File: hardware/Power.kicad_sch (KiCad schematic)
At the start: 37 parts, among them U10 LDK320ADU120R, U4 TPS563300DRLR, U5 TPS563219ADDFR, U6 LM2940SX-12_NOPB, U7 LM1117IMP-5.0, U8 TLV743P, U9 AP2127N3-1.5

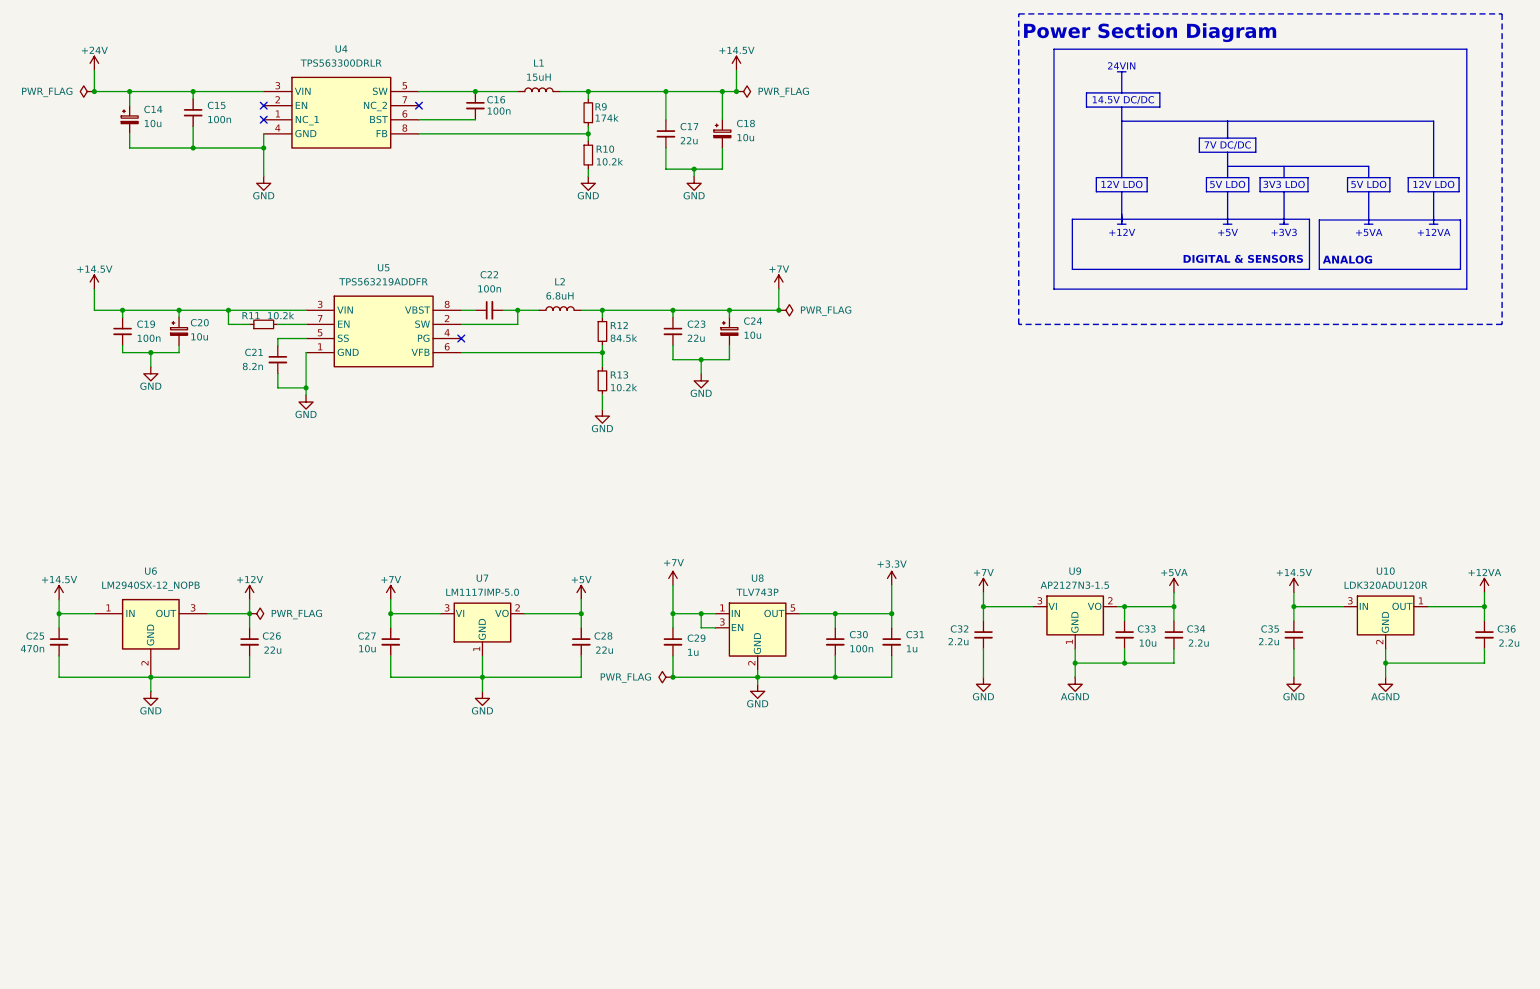
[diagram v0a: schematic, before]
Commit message: Finished components placement on PCB
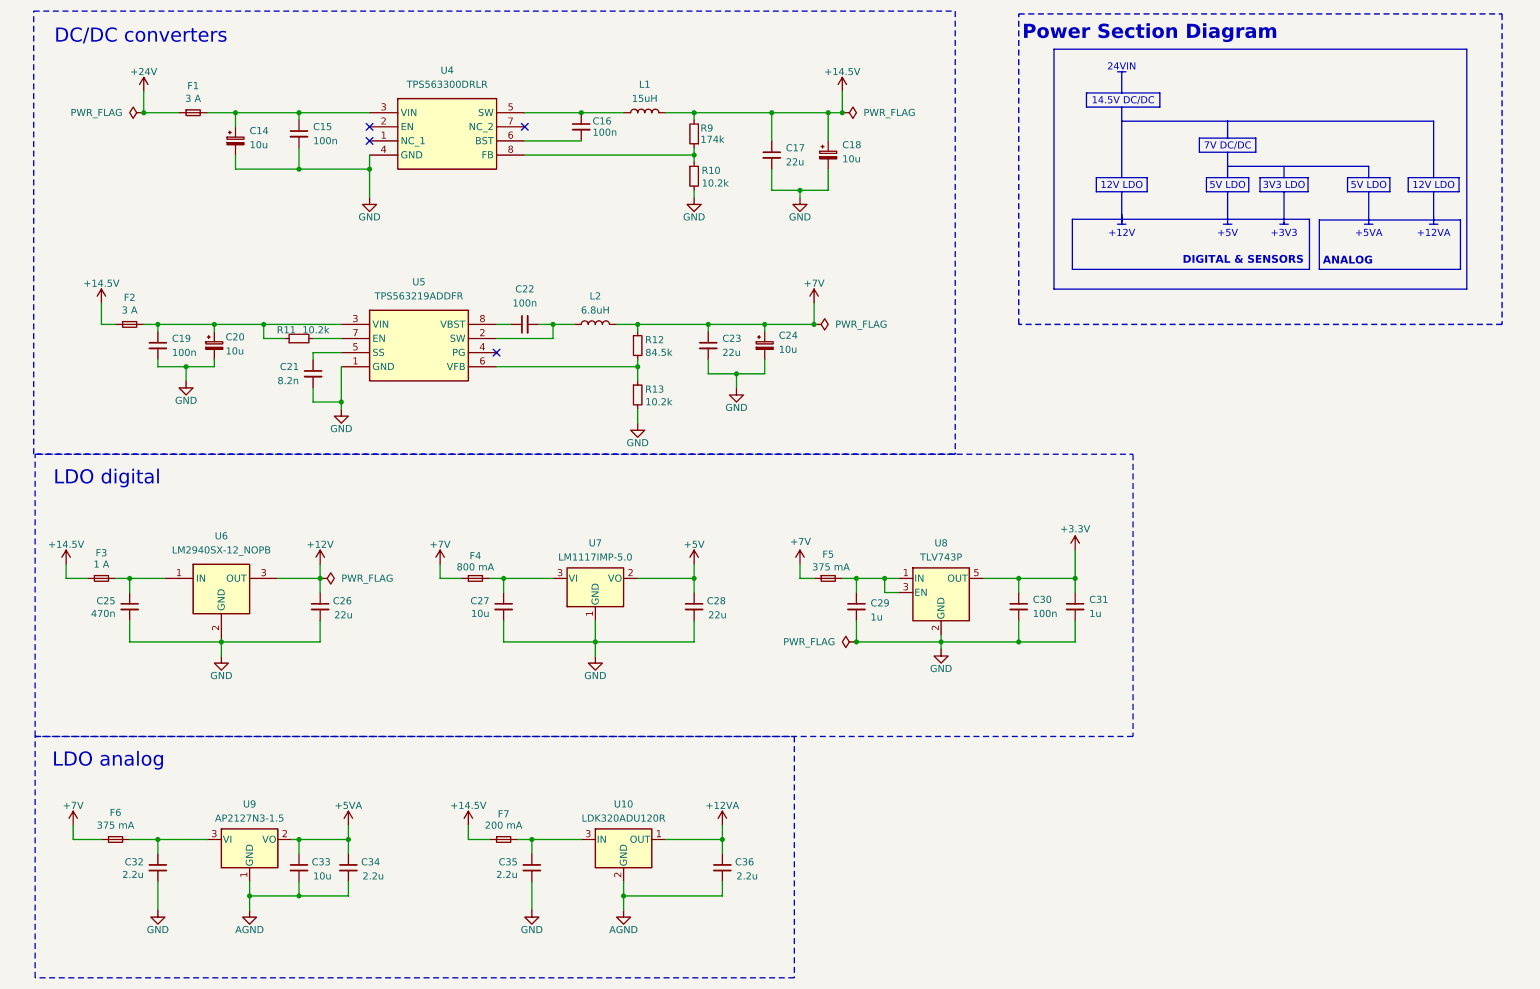
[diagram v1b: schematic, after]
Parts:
- added F1, F2: 3 A, fuse 1206:FUSC3215X66N, symbol Device:Fuse_Small
- added F3: 1 A, fuse 1206:FUSC3215X66N, symbol Device:Fuse_Small
- added F4: 800 mA, fuse 0603:FUSC1608X55N, symbol Device:Fuse_Small
- added F5, F6: 375 mA, fuse 1206:FUSC3215X66N, symbol Device:Fuse_Small
- added F7: 200 mA, fuse 1206:FUSC3215X66N, symbol Device:Fuse_Small
- L2: footprint inductor:VLS5045EX330M -> inductor 68uh:VLS5045EX330M; Manufacturer_Part_Number 104CDMCCDS-150MC -> VLS5045EX-6R8M; Mouser https://www.mouser.pl/ProductDetail/Sumida/104CDMCCDS-150MC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 -> https://www.mouser.pl/ProductDetail/TDK/VLS5045EX-6R8M?qs=o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; Mouser No 851-104CDMCCDS-150MC -> 810-VLS5045EX-6R8M
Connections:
- net +14.5V: now also F2.1, F3.1, F7.1; no longer C19.1, C20.1, C25.1, C35.1, R11.1, U10.3 (IN), U5.3 (VIN), U6.1 (IN)
- net +24V: now also F1.1; no longer C14.1, C15.1, U4.3 (VIN)
- net +7V: now also F4.1, F5.1, F6.1; no longer C27.1, C29.1, C32.1, U7.3 (VI), U8.1 (IN), U8.3 (EN), U9.3 (VI)
- new net: C27.1, F4.2, U7.3 (VI)
- new net: C19.1, C20.1, F2.2, R11.1, U5.3 (VIN)
- new net: C35.1, F7.2, U10.3 (IN)
- new net: C25.1, F3.2, U6.1 (IN)
- new net: C14.1, C15.1, F1.2, U4.3 (VIN)
- new net: C32.1, F6.2, U9.3 (VI)
- new net: C29.1, F5.2, U8.1 (IN), U8.3 (EN)
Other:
- note added: "DC/DC converters"
- note added: "LDO analog"
- note added: "LDO digital"
- moved on the sheet: C14, C15, C16, C17, C18, C19, C20, C21, C22, C23, C24, C25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

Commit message: Finished routing on PCB
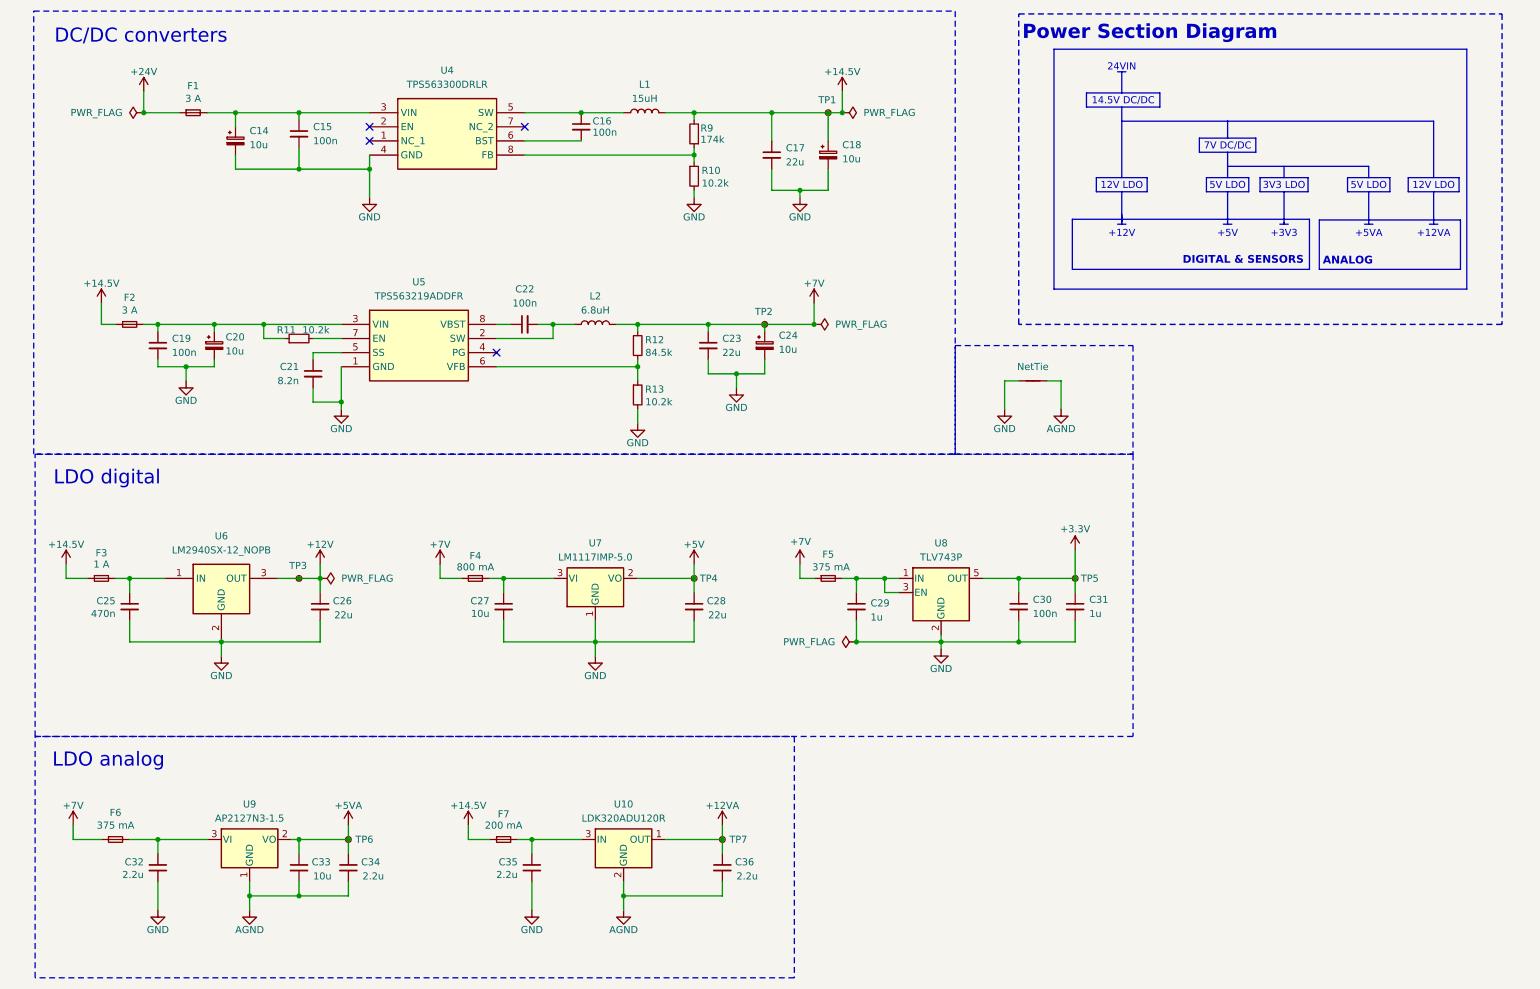
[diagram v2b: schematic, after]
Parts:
- added NT1: NetTie, NetTie:NetTie-4_THT_Pad1.0mm, symbol Device:NetTie_2
- added TP1, TP2, TP3, TP4, TP5, TP6, TP7: TestPoint_Small, TestPoint:TestPoint_THTPad_D1.0mm_Drill0.5mm, symbol Connector:TestPoint_Small
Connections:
- net +12V: now also TP3.1
- net +12VA: now also TP7.1
- net +14.5V: now also TP1.1
- net +3.3V: now also TP5.1
- net +5V: now also TP4.1
- net +5VA: now also TP6.1
- net +7V: now also TP2.1
- net AGND: now also NT1.2
- net GND: now also NT1.1

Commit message: Added all missing datasheet links etc
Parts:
- TP1, TP2, TP3, TP4, TP5, TP6, TP7: Manufacturer_Part_Number (none) -> ---; Mouser (none) -> ---; Mouser No (none) -> ---
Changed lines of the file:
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@@
 			)
 		)
+		(property "Manufacturer_Part_Number" "---"
+			(at 72.39 166.37 0)
+			(effects
+				(font
+					(size 1.27 1.27)
+				)
+				(hide yes)
+			)
+		)
+		(property "Mouser" "---"
+			(at 72.39 166.37 0)
+			(effects
+				(font
+					(size 1.27 1.27)
+				)
+				(hide yes)
+			)
+		)
+		(property "Mouser No" "---"
+			(at 72.39 166.37 0)
+			(effects
+				(font
+					(size 1.27 1.27)
+				)
+				(hide yes)
+			)
+		)
 		(pin "1"
 		)
@@
 			)
 		)
+		(property "Manufacturer_Part_Number" "---"
+			(at 203.2 119.38 0)
+			(effects
+				(font
+					(size 1.27 1.27)
+				)
+				(hide yes)
+			)
+		)
+		(property "Mouser" "---"
+			(at 203.2 119.38 0)
+			(effects
+				(font
+					(size 1.27 1.27)
+				)
+				(hide yes)
+			)
+		)
+		(property "Mouser No" "---"
+			(at 203.2 119.38 0)
+			(effects
+				(font
+					(size 1.27 1.27)
+				)
+				(hide yes)
+			)
+		)
 		(pin "1"
 		)
@@
 			)
 		)
+		(property "Manufacturer_Part_Number" "---"
+			(at 158.75 35.56 0)
+			(effects
+				(font
+					(size 1.27 1.27)
+				)
+				(hide yes)
+			)
+		)
+		(property "Mouser" "---"
+			(at 158.75 35.56 0)
+			(effects
+				(font
+					(size 1.27 1.27)
+				)
+				(hide yes)
+			)
+		)
+		(property "Mouser No" "---"
+			(at 158.75 35.56 0)
+			(effects
+				(font
+					(size 1.27 1.27)
+				)
+				(hide yes)
+			)
+		)
 		(pin "1"
 		)
@@
 			)
 		)
+		(property "Manufacturer_Part_Number" "---"
+			(at 134.62 119.38 0)
+			(effects
+				(font
+					(size 1.27 1.27)
+				)
+				(hide yes)
+			)
+		)
+		(property "Mouser" "---"
+			(at 134.62 119.38 0)
+			(effects
+				(font
+					(size 1.27 1.27)
+				)
+				(hide yes)
+			)
+		)
+		(property "Mouser No" "---"
+			(at 134.62 119.38 0)
+			(effects
+				(font
+					(size 1.27 1.27)
+				)
+				(hide yes)
+			)
+		)
 		(pin "1"
 		)
@@
 			)
 		)
+		(property "Manufacturer_Part_Number" "---"
+			(at 139.7 166.37 0)
+			(effects
+				(font
+					(size 1.27 1.27)
+				)
+				(hide yes)
+			)
+		)
+		(property "Mouser" "---"
+			(at 139.7 166.37 0)
+			(effects
+				(font
+					(size 1.27 1.27)
+				)
+				(hide yes)
+			)
+		)
+		(property "Mouser No" "---"
+			(at 139.7 166.37 0)
+			(effects
+				(font
+					(size 1.27 1.27)
+				)
+				(hide yes)
+			)
+		)
 		(pin "1"
 		)
@@
 			)
 		)
+		(property "Manufacturer_Part_Number" "---"
+			(at 147.32 73.66 0)
+			(effects
+				(font
+					(size 1.27 1.27)
+				)
+				(hide yes)
+			)
+		)
+		(property "Mouser" "---"
+			(at 147.32 73.66 0)
+			(effects
+				(font
+					(size 1.27 1.27)
+				)
+				(hide yes)
+			)
+		)
+		(property "Mouser No" "---"
+			(at 147.32 73.66 0)
+			(effects
+				(font
+					(size 1.27 1.27)
+				)
+				(hide yes)
+			)
+		)
 		(pin "1"
 		)
@@
 			(at 63.5 119.38 0)
 			(effects
+				(font
+					(size 1.27 1.27)
+				)
+				(hide yes)
+			)
+		)
+		(property "Manufacturer_Part_Number" "---"
+			(at 63.5 119.38 0)
+			(effects
+				(font
+					(size 1.27 1.27)
+				)
+				(hide yes)
+			)
+		)
+		(property "Mouser" "---"
+			(at 63.5 119.38 0)
+			(effects
+				(font
+					(size 1.27 1.27)
+				)
+				(hide yes)
+			)
+		)
+		(property "Mouser No" "---"
+			(at 63.5 119.38 0)
+			(effects

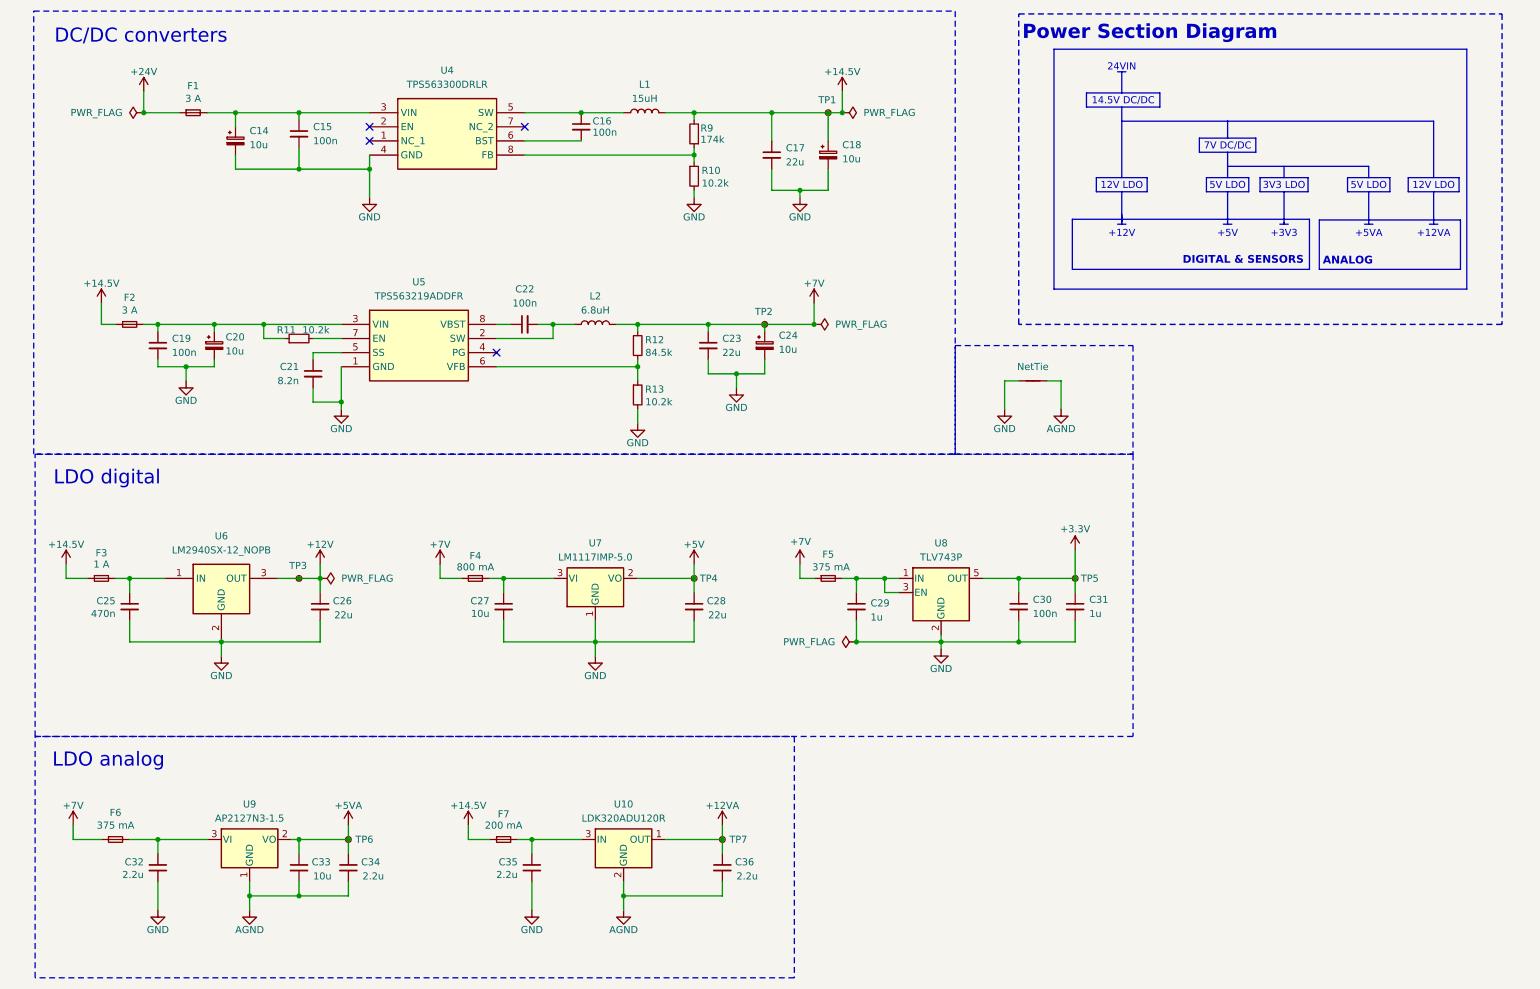
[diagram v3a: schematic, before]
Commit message: Corrections after review
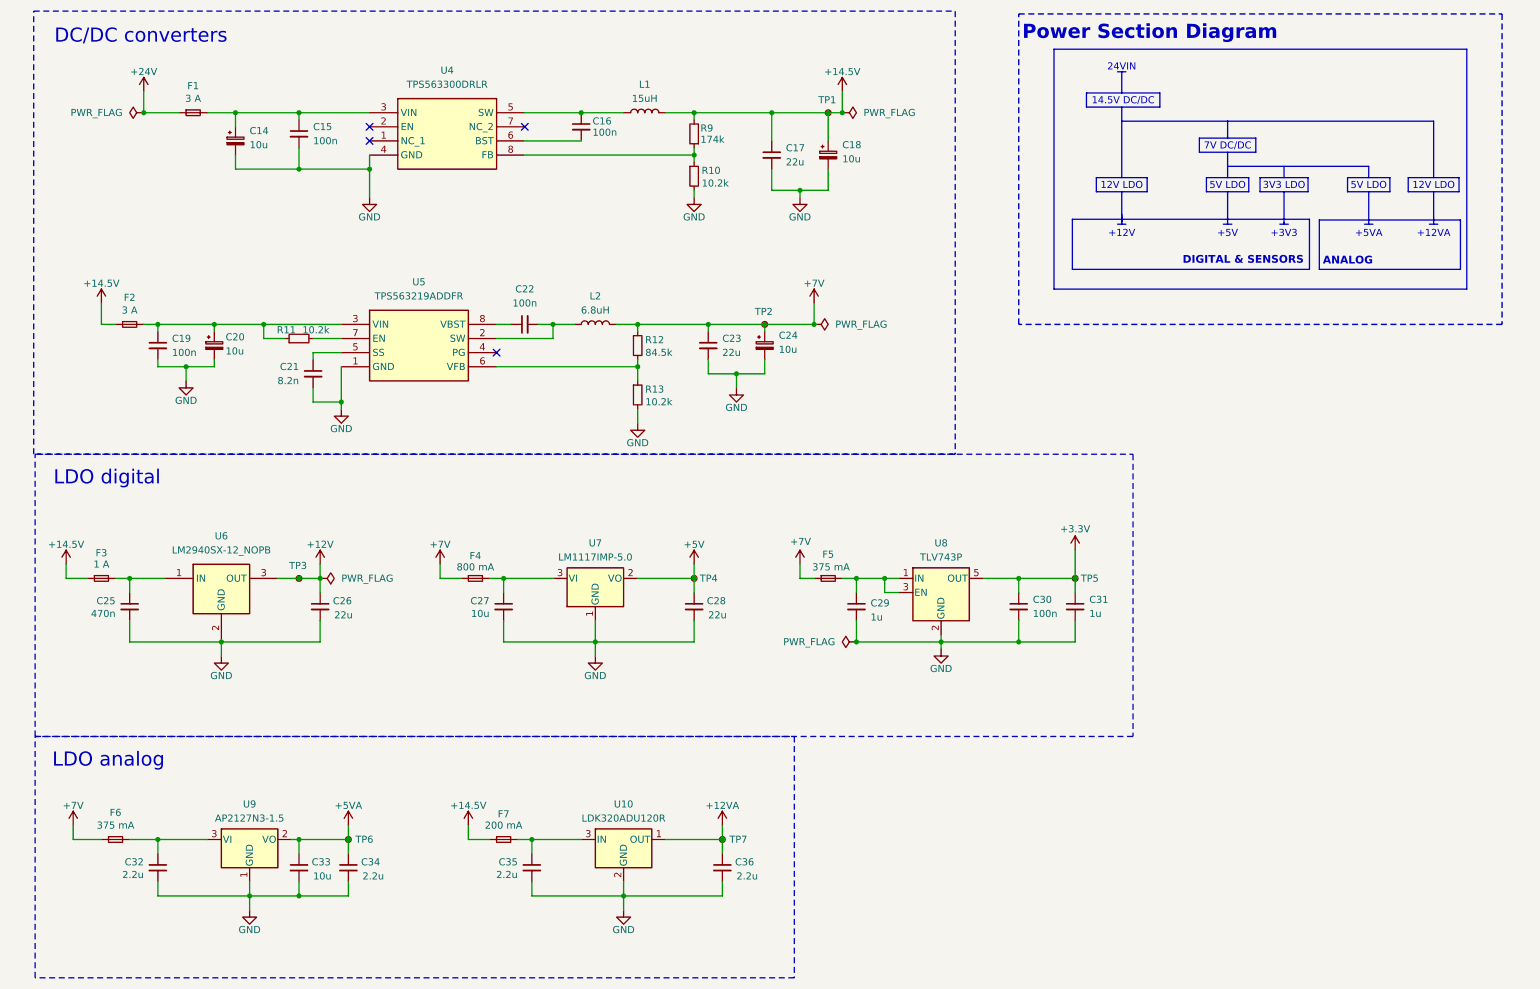
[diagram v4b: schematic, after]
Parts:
- removed NT1: NetTie, NetTie:NetTie-4_THT_Pad1.0mm, symbol Device:NetTie_2
- TP1, TP2, TP3, TP4, TP5, TP6, TP7: Manufacturer_Part_Number --- -> (none); Mouser --- -> (none); Mouser No --- -> (none)
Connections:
- net AGND is gone; now on net GND: C33.2, C34.2, C36.2, U10.2 (GND), U9.1 (GND)

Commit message: Added description, fixed engineering fee
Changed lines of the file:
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@@
 	)
 	(junction
-		(at 163.83 130.81)
-		(diameter 0)
-		(color 0 0 0 0)
-	)
-	(junction
 		(at 33.02 119.38)
 		(diameter 0)
@@
 					(unit 1)
 				)
-			)
-		)
-	)
-	(symbol
-		(lib_id "power:PWR_FLAG")
-		(at 163.83 130.81 90)
-		(unit 1)
-		(exclude_from_sim no)
-		(in_bom yes)
-		(on_board yes)
-		(dnp no)
-		(fields_autoplaced yes)
-		(property "Reference" "#FLG014"
-			(at 161.925 130.81 0)
-			(effects
-				(font
-					(size 1.27 1.27)
-				)
-				(hide yes)
-			)
-		)
-		(property "Value" "PWR_FLAG"
-			(at 160.02 130.8099 90)
-			(effects
-				(font
-					(size 1.27 1.27)
-				)
-				(justify left)
-			)
-		)
-		(property "Footprint" ""
-			(at 163.83 130.81 0)
-			(effects
-				(font
-					(size 1.27 1.27)
-				)
-				(hide yes)
-			)
-		)
-		(property "Datasheet" "~"
-			(at 163.83 130.81 0)
-			(effects
-				(font
-					(size 1.27 1.27)
-				)
-				(hide yes)
-			)
-		)
-		(property "Description" "Special symbol for telling ERC where power comes from"
-			(at 163.83 130.81 0)
-			(effects
-				(font
-					(size 1.27 1.27)
-				)
-				(hide yes)
-			)
-		)
-		(pin "1"
-		)
-		(instances
-			(project ""
-				(path "/b652b05a-4e3d-4ad1-b032-18886abe7d45/d6d0b9a5-d6bd-4532-a3f2-84b92b0fd444"
-					(reference "#FLG014")
-					(unit 1)
-				)
